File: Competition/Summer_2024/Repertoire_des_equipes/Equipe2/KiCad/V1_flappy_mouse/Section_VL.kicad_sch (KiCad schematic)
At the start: 0 parts

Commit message: starting the pin out of the ESP32
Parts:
- added J1, J2: Conn_01x22_Pin, symbol Connector:Conn_01x22_Pin
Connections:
- new net +3.3V: J2.1 (Pin_1), J2.2 (Pin_2)
- new net +5V: J2.21 (Pin_21)
- new net GND: J1.1 (Pin_1), J1.21 (Pin_21), J1.22 (Pin_22), J2.22 (Pin_22)
- new net GPIO/RTC/TOUCH1/ADC1_0: J1.4 (Pin_4)
- new net U0RXD/GPIO44/CLK_OUT2: J1.3 (Pin_3)
- new net U0TXD/GPIO43/CLK_OUT1: J1.2 (Pin_2)

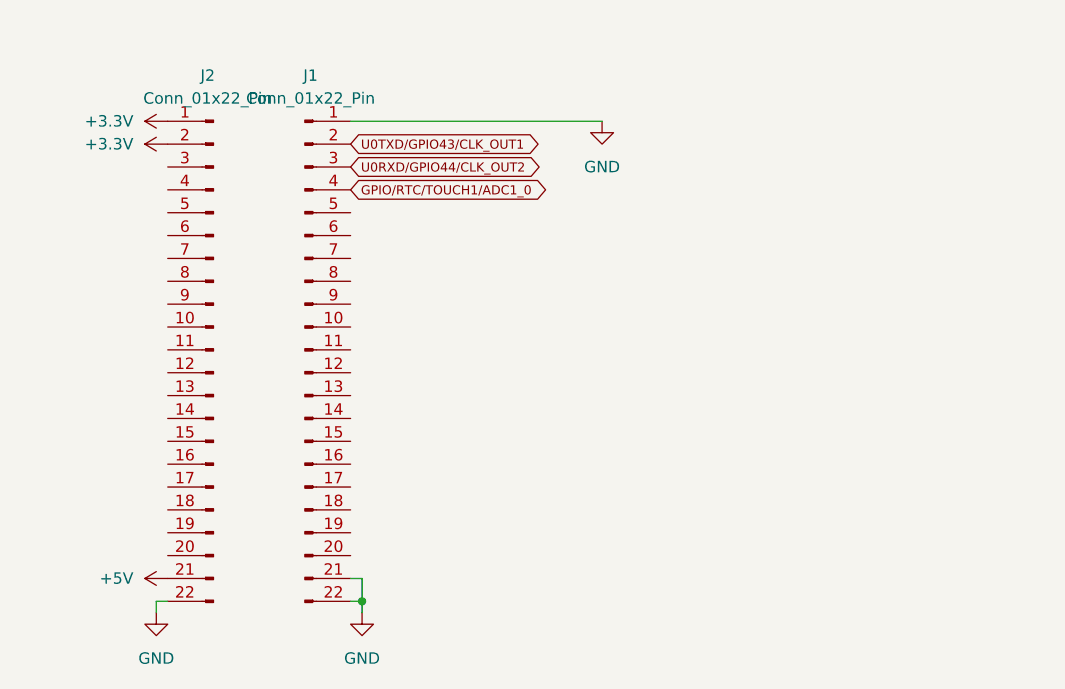
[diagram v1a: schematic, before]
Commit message: apply change for the pinout
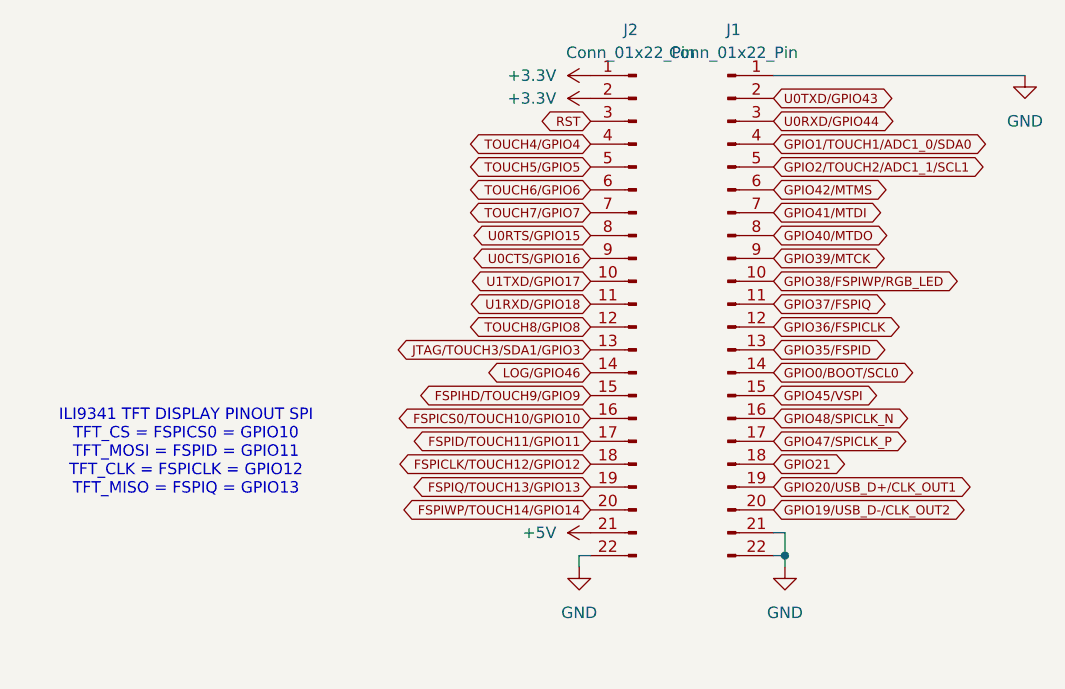
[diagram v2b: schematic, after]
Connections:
- net U1TXD/GPIO17: now reaches J2.10 (Pin_10)
- net U1RXD/GPIO18: now reaches J2.11 (Pin_11)
- net TOUCH8/GPIO8: now reaches J2.12 (Pin_12)
- net JTAG/TOUCH3/SDA1/GPIO3: now reaches J2.13 (Pin_13)
- net LOG/GPIO46: now reaches J2.14 (Pin_14)
- net FSPIHD/TOUCH9/GPIO9: now reaches J2.15 (Pin_15)
- net FSPICS0/TOUCH10/GPIO10: now reaches J2.16 (Pin_16)
- net FSPID/TOUCH11/GPIO11: now reaches J2.17 (Pin_17)
- net FSPICLK/TOUCH12/GPIO12: now reaches J2.18 (Pin_18)
- net FSPIQ/TOUCH13/GPIO13: now reaches J2.19 (Pin_19)
- net FSPIWP/TOUCH14/GPIO14: now reaches J2.20 (Pin_20)
- net RST: now reaches J2.3 (Pin_3)
- net TOUCH4/GPIO4: now reaches J2.4 (Pin_4)
- net TOUCH5/GPIO5: now reaches J2.5 (Pin_5)
- net TOUCH6/GPIO6: now reaches J2.6 (Pin_6)
- net TOUCH7/GPIO7: now reaches J2.7 (Pin_7)
- net U0RTS/GPIO15: now reaches J2.8 (Pin_8)
- net U0CTS/GPIO16: now reaches J2.9 (Pin_9)
- net GPIO38/FSPIWP/RGB_LED: now reaches J1.10 (Pin_10)
- net GPIO37/FSPIQ: now reaches J1.11 (Pin_11)
- net GPIO36/FSPICLK: now reaches J1.12 (Pin_12)
- net GPIO35/FSPID: now reaches J1.13 (Pin_13)
- net GPIO0/BOOT/SCL0: now reaches J1.14 (Pin_14)
- net GPIO45/VSPI: now reaches J1.15 (Pin_15)
- net GPIO48/SPICLK_N: now reaches J1.16 (Pin_16)
- net GPIO47/SPICLK_P: now reaches J1.17 (Pin_17)
- net GPIO21: now reaches J1.18 (Pin_18)
- net GPIO20/USB_D+/CLK_OUT1: now reaches J1.19 (Pin_19)
- net GPIO19/USB_D-/CLK_OUT2: now reaches J1.20 (Pin_20)
- net GPIO2/TOUCH2/ADC1_1/SCL1: now reaches J1.5 (Pin_5)
- net GPIO42/MTMS: now reaches J1.6 (Pin_6)
- net GPIO41/MTDI: now reaches J1.7 (Pin_7)
- net GPIO40/MTDO: now reaches J1.8 (Pin_8)
- net GPIO39/MTCK: now reaches J1.9 (Pin_9)
- net GPIO/RTC/TOUCH1/ADC1_0 renamed GPIO1/TOUCH1/ADC1_0/SDA0
- net U0RXD/GPIO44/CLK_OUT2 renamed U0RXD/GPIO44
- net U0TXD/GPIO43/CLK_OUT1 renamed U0TXD/GPIO43
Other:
- note added: "ILI9341 TFT DISPLAY PINOUT SPI TFT_CS = FSPICS0 = GPIO10 TFT_MOSI = FSPID = GPIO11 TFT_CLK = FSPICLK = GPIO12 TFT_MISO = FSPIQ = GPIO13"
- moved on the sheet: J1, J2

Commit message: quick note of the pinout of the LCD display
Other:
- note added: "PINOUT OF THE TFT DISPLAY (CHIP ST7789) GND = GND VCC = 3.3V SCL = CLK = FSPICLK SDA = MOSI = FSPID RES = FSPIHD DC = FSPIWP CS = CS = FSPICS0 BLK = NOTHING (USELESS)"
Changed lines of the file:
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@@
+		)
+	)
+	(text "PINOUT OF THE TFT DISPLAY (CHIP ST7789)\nGND = GND\nVCC = 3.3V\nSCL = CLK = FSPICLK\nSDA = MOSI = FSPID\nRES = FSPIHD \nDC = FSPIWP\nCS = CS = FSPICS0\nBLK = NOTHING (USELESS)"
+		(exclude_from_sim no)
+		(at 42.672 102.87 0)
+		(effects
+			(font
+				(size 1.27 1.27)
+			)
 		)
 	)
@@
 		)
 	)
+	(sheet_instances
+		(path "/"
+			(page "1")
+		)
+	)

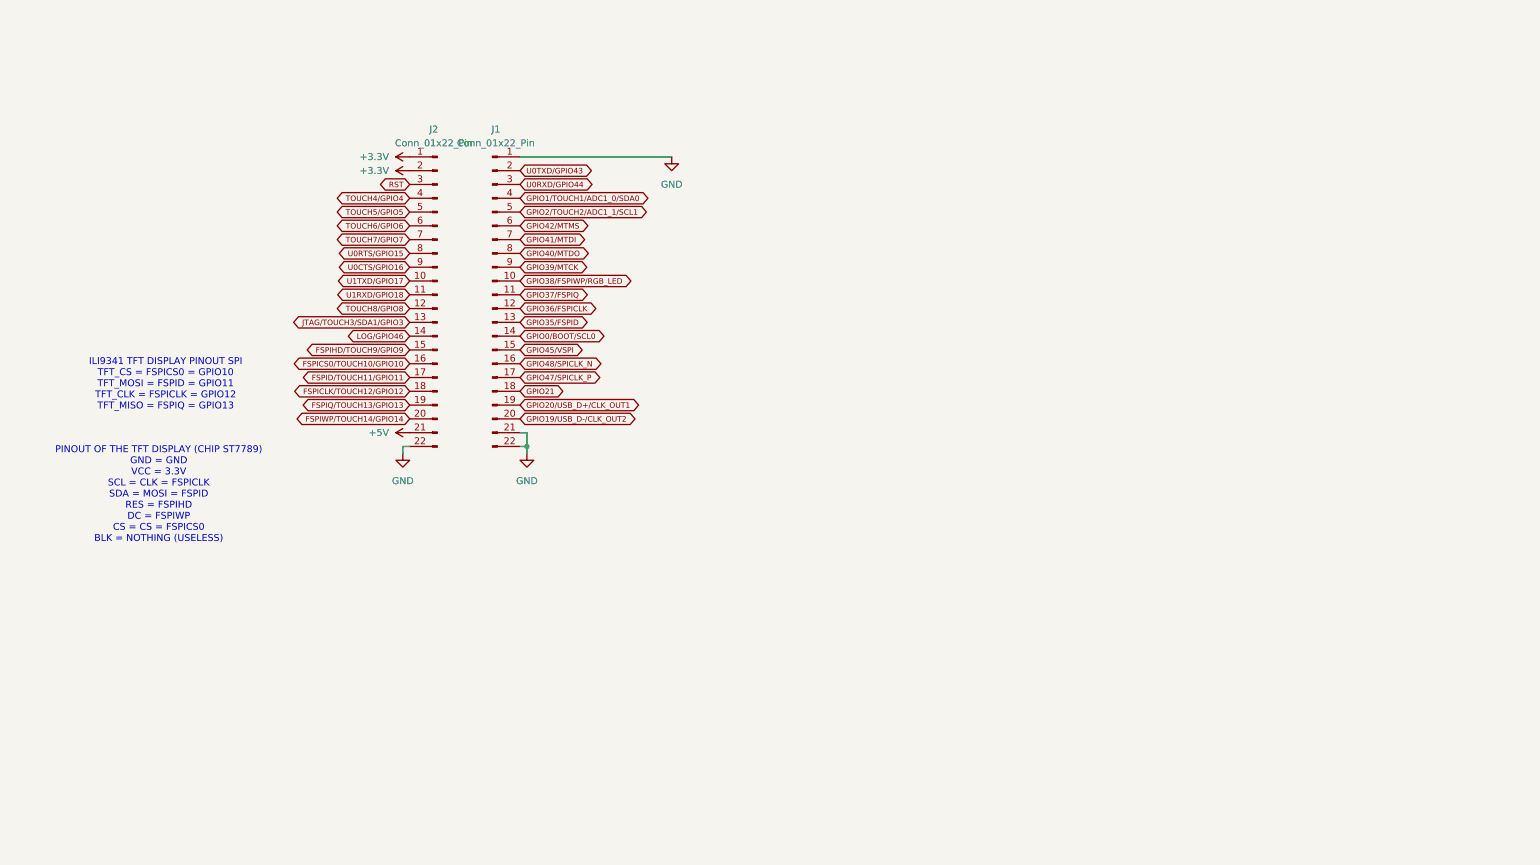
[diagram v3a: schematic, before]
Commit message: add pinout of TFT screen and the circuit for the sound sensor
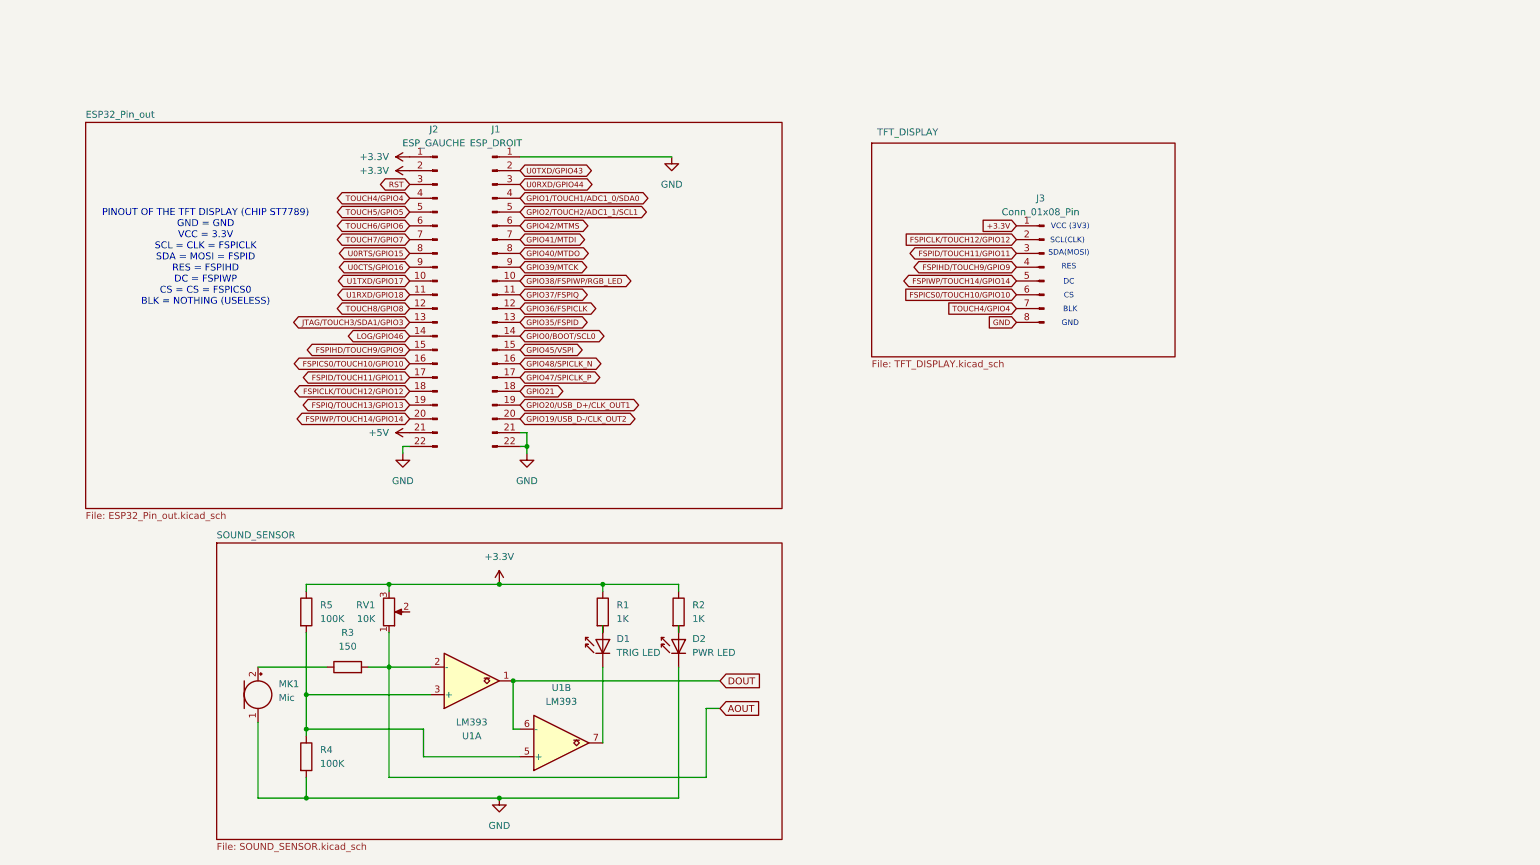
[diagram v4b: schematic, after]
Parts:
- added D1: TRIG LED, LED_THT:LED_D5.0mm_IRGrey, symbol LED:SFH4550
- added D2: PWR LED, LED_THT:LED_D5.0mm_IRGrey, symbol LED:SFH4550
- added J3: Conn_01x08_Pin, symbol Connector:Conn_01x08_Pin
- added MK1: Mic, symbol Device:Microphone
- added R1, R2: 1K, symbol Device:R
- added R3: 150, symbol Device:R
- added R4, R5: 100K, symbol Device:R
- added RV1: 10K, symbol Device:R_Potentiometer
- added U1: LM393, symbol Comparator:LM393
- J1: value Conn_01x22_Pin -> ESP_DROIT
- J2: value Conn_01x22_Pin -> ESP_GAUCHE
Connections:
- net +3.3V: now also J3.1 (Pin_1), R1.1, R2.1, R5.1, RV1.3
- net FSPICLK/TOUCH12/GPIO12: now also J3.2 (Pin_2)
- net FSPICS0/TOUCH10/GPIO10: now also J3.6 (Pin_6)
- net FSPID/TOUCH11/GPIO11: now also J3.3 (Pin_3)
- net FSPIHD/TOUCH9/GPIO9: now also J3.4 (Pin_4)
- net FSPIWP/TOUCH14/GPIO14: now also J3.5 (Pin_5)
- net GND: now also D2.1 (K), J3.8 (Pin_8), MK1.1 (-), R4.2
- net TOUCH4/GPIO4: now also J3.7 (Pin_7)
- new net: R4.1, R5.2, U1.3 (+), U1.5 (+)
- new net: MK1.2 (+), R3.1
- new net: D2.2 (A), R2.2
- new net: D1.2 (A), R1.2
- new net: D1.1 (K), U1.7
- new net AOUT: R3.2, RV1.1, U1.2 (-)
- new net DOUT: U1.1, U1.6 (-)
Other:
- added sheet ESP32_Pin_out (ESP32_Pin_out.kicad_sch)
- added sheet SOUND_SENSOR (SOUND_SENSOR.kicad_sch)
- added sheet TFT_DISPLAY (TFT_DISPLAY.kicad_sch)
- note added: "BLK"
- note added: "CS"
- note added: "DC"
- note added: "GND"
- note added: "RES"
- note added: "SCL(CLK)"
- note added: "SDA(MOSI)"
- note added: "VCC (3V3)"
- note removed: "ILI9341 TFT DISPLAY PINOUT SPI TFT_CS = FSPICS0 = GPIO10 TFT_MOSI = FSPID = GPIO11 TFT_CLK = FSPICLK = GPIO12 TFT_MISO = FSPIQ = GPIO13"

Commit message: change pinout of the LCD
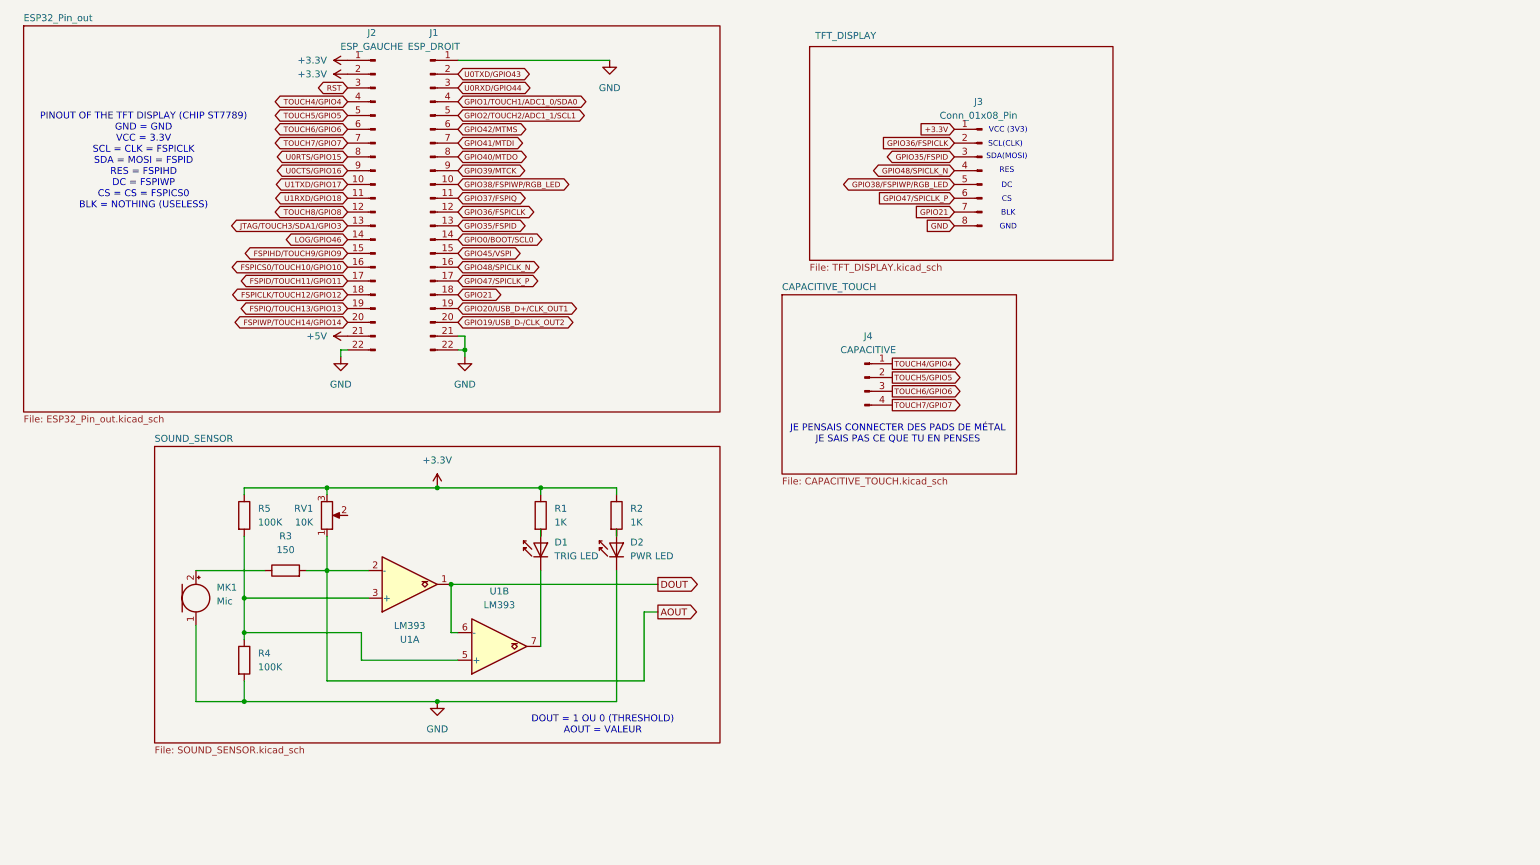
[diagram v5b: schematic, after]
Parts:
- added J4: CAPACITIVE, symbol Connector:Conn_01x04_Pin
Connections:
- net FSPICLK/TOUCH12/GPIO12: no longer J3.2 (Pin_2)
- net FSPICS0/TOUCH10/GPIO10: no longer J3.6 (Pin_6)
- net FSPID/TOUCH11/GPIO11: no longer J3.3 (Pin_3)
- net FSPIHD/TOUCH9/GPIO9: no longer J3.4 (Pin_4)
- net FSPIWP/TOUCH14/GPIO14: no longer J3.5 (Pin_5)
- net GPIO21: now also J3.7 (Pin_7)
- net GPIO35/FSPID: now also J3.3 (Pin_3)
- net GPIO36/FSPICLK: now also J3.2 (Pin_2)
- net GPIO38/FSPIWP/RGB_LED: now also J3.5 (Pin_5)
- net GPIO47/SPICLK_P: now also J3.6 (Pin_6)
- net GPIO48/SPICLK_N: now also J3.4 (Pin_4)
- net TOUCH4/GPIO4: now also J4.1 (Pin_1); no longer J3.7 (Pin_7)
- net TOUCH5/GPIO5: now also J4.2 (Pin_2)
- net TOUCH6/GPIO6: now also J4.3 (Pin_3)
- net TOUCH7/GPIO7: now also J4.4 (Pin_4)
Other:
- added sheet CAPACITIVE_TOUCH (CAPACITIVE_TOUCH.kicad_sch)
- note added: "DOUT = 1 OU 0 (THRESHOLD) AOUT = VALEUR"
- note added: "JE PENSAIS CONNECTER DES PADS DE MÉTAL JE SAIS PAS CE QUE TU EN PENSES"
- moved on the sheet: D1, D2, J1, J2, J3, MK1, R1, R2, R3, R4, R5, RV1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
